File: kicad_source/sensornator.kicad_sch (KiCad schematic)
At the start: 23 parts, among them CN1 ARDUINO, CON1 Micro_SDCard, SW1 TAST_VER, SW2 TAST_VER, U5 ESP32_WROOM_32, U6 ATECC608A

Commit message: added qwiic connector
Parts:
- added CN2: SM04B-SRSS-TB, Connector_JST:JST_SH_SM04B-SRSS-TB_1x04-1MP_P1.00mm_Horizontal, symbol Connector_Generic:Conn_01x04
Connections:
- net +3V3: now also CN2.2 (Pin_2)
- net GND: now also CN2.1 (Pin_1)
- net I2C_SCL: now also CN2.4 (Pin_4)
- net I2C_SDA: now also CN2.3 (Pin_3)
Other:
- note added: "Copyright generationmake 2022 see full project documentation at https://github.com/generationmake/sensornator"
- note removed: "Copyright generationmake 2021 see full project documentation at https://github.com/generationmake/sensornator"
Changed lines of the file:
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@@
+    (stroke (width 0) (type default) (color 0 0 0 0))
+  )
+  (wire (pts (xy 73.66 41.91) (xy 97.79 41.91))
     (stroke (width 0) (type default) (color 0 0 0 0))
   )
@@
     (stroke (width 0) (type default) (color 0 0 0 0))
   )
+  (wire (pts (xy 92.71 39.37) (xy 92.71 34.29))
+    (stroke (width 0) (type default) (color 0 0 0 0))
+  )
   (wire (pts (xy 260.35 115.57) (xy 260.35 114.3))
     (stroke (width 0) (type default) (color 0 0 0 0))
@@
     (stroke (width 0) (type default) (color 0 0 0 0))
   )
+  (wire (pts (xy 97.79 39.37) (xy 92.71 39.37))
+    (stroke (width 0) (type default) (color 0 0 0 0))
+  )
   (wire (pts (xy 111.76 152.4) (xy 111.76 151.13))
     (stroke (width 0) (type default) (color 0 0 0 0))
@@
     (stroke (width 0) (type default) (color 0 0 0 0))
   )
+  (wire (pts (xy 97.79 36.83) (xy 95.25 36.83))
+    (stroke (width 0) (type default) (color 0 0 0 0))
+  )
   (wire (pts (xy 212.09 105.41) (xy 196.85 105.41))
     (stroke (width 0) (type default) (color 0 0 0 0))
@@
     (stroke (width 0) (type default) (color 0 0 0 0))
   )
+  (wire (pts (xy 73.66 44.45) (xy 97.79 44.45))
+    (stroke (width 0) (type default) (color 0 0 0 0))
+  )
   (wire (pts (xy 217.17 92.71) (xy 227.33 92.71))
     (stroke (width 0) (type default) (color 0 0 0 0))
@@
     (stroke (width 0) (type default) (color 0 0 0 0))
   )
+  (wire (pts (xy 95.25 36.83) (xy 95.25 46.99))
+    (stroke (width 0) (type default) (color 0 0 0 0))
+  )
   (wire (pts (xy 247.65 95.25) (xy 266.7 95.25))
     (stroke (width 0) (type default) (color 0 0 0 0))
@@
     (stroke (width 0) (type default) (color 0 0 0 0))
   )
-  (text "Copyright generationmake 2021\nsee full project documentation at https://github.com/generationmake/sensornator"
+  (text "Copyright generationmake 2022\nsee full project documentation at https://github.com/generationmake/sensornator"
     (at 12.7 16.51 0)
     (effects (font (size 1.1938 1.1938)) (justify left bottom))
@@
     (effects (font (size 1.524 1.524)) (justify left bottom))
   )
+  (label "I2C_SDA" (at 76.2 41.91 0)
+    (effects (font (size 1.524 1.524)) (justify left bottom))
+  )
   (label "EXT_RX" (at 250.19 85.09 0)
     (effects (font (size 1.524 1.524)) (justify left bottom))
@@
   )
   (label "ADC_1" (at 143.51 107.95 0)
+    (effects (font (size 1.524 1.524)) (justify left bottom))
+  )
+  (label "I2C_SCL" (at 76.2 44.45 0)
     (effects (font (size 1.524 1.524)) (justify left bottom))
   )
@@
     (pin "1")
   )
+  (symbol (lib_id "power:GND") (at 95.25 46.99 0) (unit 1)
+    (in_bom yes) (on_board yes)
+    (property "Reference" "#PWR012" (id 0) (at 95.25 53.34 0)
+      (effects (font (size 1.27 1.27)) hide)
+    )
+    (property "Value" "GND" (id 1) (at 95.25 50.8 0))
+    (property "Footprint" "" (id 2) (at 95.25 46.99 0))
+    (property "Datasheet" "" (id 3) (at 95.25 46.99 0))
+    (pin "1")
+  )
+  (symbol (lib_id "power:+3V3") (at 92.71 34.29 0) (unit 1)
+    (in_bom yes) (on_board yes)
+    (property "Reference" "#PWR011" (id 0) (at 92.71 38.1 0)
+      (effects (font (size 1.27 1.27)) hide)
+    )
+    (property "Value" "+3V3" (id 1) (at 93.091 31.0388 90)
+      (effects (font (size 1.27 1.27)) (justify left))
+    )
+    (property "Footprint" "" (id 2) (at 92.71 34.29 0))
+    (property "Datasheet" "" (id 3) (at 92.71 34.29 0))
+    (pin "1")
+  )
+  (symbol (lib_id "Connector_Generic:Conn_01x04") (at 102.87 39.37 0) (unit 1)
+    (in_bom yes) (on_board yes) (fields_autoplaced)
+    (property "Reference" "CN2" (id 0) (at 105.41 39.3699 0)
+      (effects (font (size 1.27 1.27)) (justify left))
+    )
+    (property "Value" "SM04B-SRSS-TB" (id 1) (at 105.41 41.9099 0)
+      (effects (font (size 1.27 1.27)) (justify left))
+    )
+    (property "Footprint" "Connector_JST:JST_SH_SM04B-SRSS-TB_1x04-1MP_P1.00mm_Horizontal" (id 2) (at 102.87 39.37 0)
+      (effects (font (size 1.27 1.27)) hide)
+    )
+    (property "Datasheet" "~" (id 3) (at 102.87 39.37 0)
+      (effects (font (size 1.27 1.27)) hide)
+    )
+    (pin "1")
+    (pin "2")
+    (pin "3")
+    (pin "4")
+  )
   (sheet (at 193.04 17.78) (size 21.59 15.24) (fields_autoplaced)
     (stroke (width 0) (type solid) (color 0 0 0 0))
@@
       (reference "#PWR010") (unit 1) (value "+3V3") (footprint "")
     )
+    (path "/723b0529-256e-4ea5-9e85-1d36b6678c46"
+      (reference "#PWR011") (unit 1) (value "+3V3") (footprint "")
+    )
+    (path "/1e42b0a4-ea04-4839-a101-ab6257e0d802"
+      (reference "#PWR012") (unit 1) (value "GND") (footprint "")
+    )
     (path "/00000000-0000-0000-0000-00005c166f4e"
       (reference "#PWR027") (unit 1) (value "GND") (footprint "")
@@
       (reference "CN1") (unit 1) (value "ARDUINO") (footprint "MODULE_compute:ARDUINO")
     )
+    (path "/f4d1e3aa-f75c-415b-af4a-76f49f7094e0"
+      (reference "CN2") (unit 1) (value "SM04B-SRSS-TB") (footprint "Connector_JST:JST_SH_SM04B-SRSS-TB_1x04-1MP_P1.00mm_Horizontal")
+    )
     (path "/00000000-0000-0000-0000-00005c166ac7"

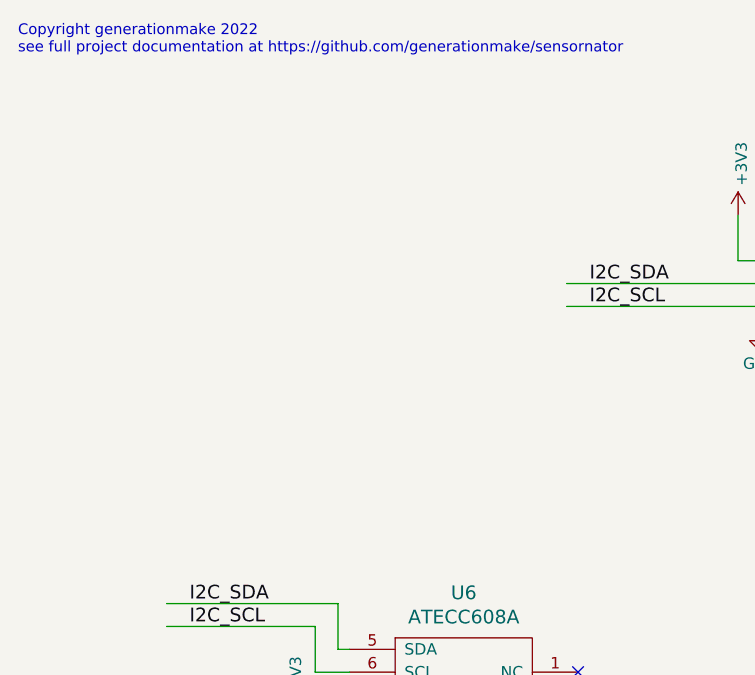
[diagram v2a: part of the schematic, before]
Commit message: added i2c eeprom
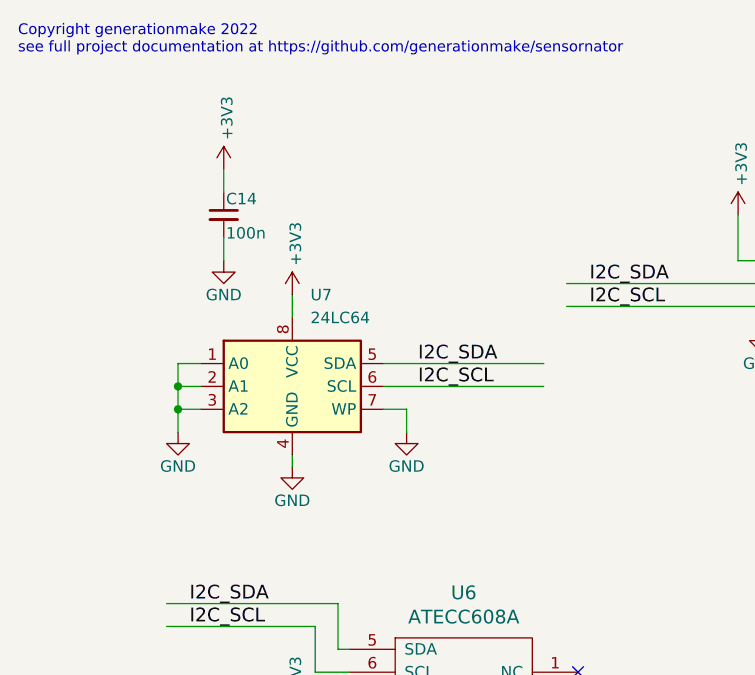
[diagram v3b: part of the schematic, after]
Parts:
- added C14: 100n, Capacitor_SMD:C_0603_1608Metric, symbol Device:C_Small
- added U7: 24LC64, Package_SO:SOIC-8_3.9x4.9mm_P1.27mm, symbol Memory_EEPROM:24LC64
- U6: footprint SOIC:SOIC-8_3.9x4.9mm_Pitch1.27mm -> Package_SO:SOIC-8_3.9x4.9mm_P1.27mm
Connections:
- net +3V3: now also C14.1, U7.8 (VCC)
- net GND: now also C14.2, U7.1 (A0), U7.2 (A1), U7.3 (A2), U7.4 (GND), U7.7 (WP)
- net I2C_SCL: now also U7.6 (SCL)
- net I2C_SDA: now also U7.5 (SDA)

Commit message: updated footprint libraries
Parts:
- C10, C11, C13, C8, C9: footprint capacitors:C_0603 -> Capacitor_SMD:C_0603_1608Metric
- D2: footprint LEDs:LED_0603 -> LED_SMD:LED_0603_1608Metric
- R11, R12, R13, R14, R15, R18, R19, R2, R20, R21, R8: footprint resistors:R_0603 -> Resistor_SMD:R_0603_1608Metric

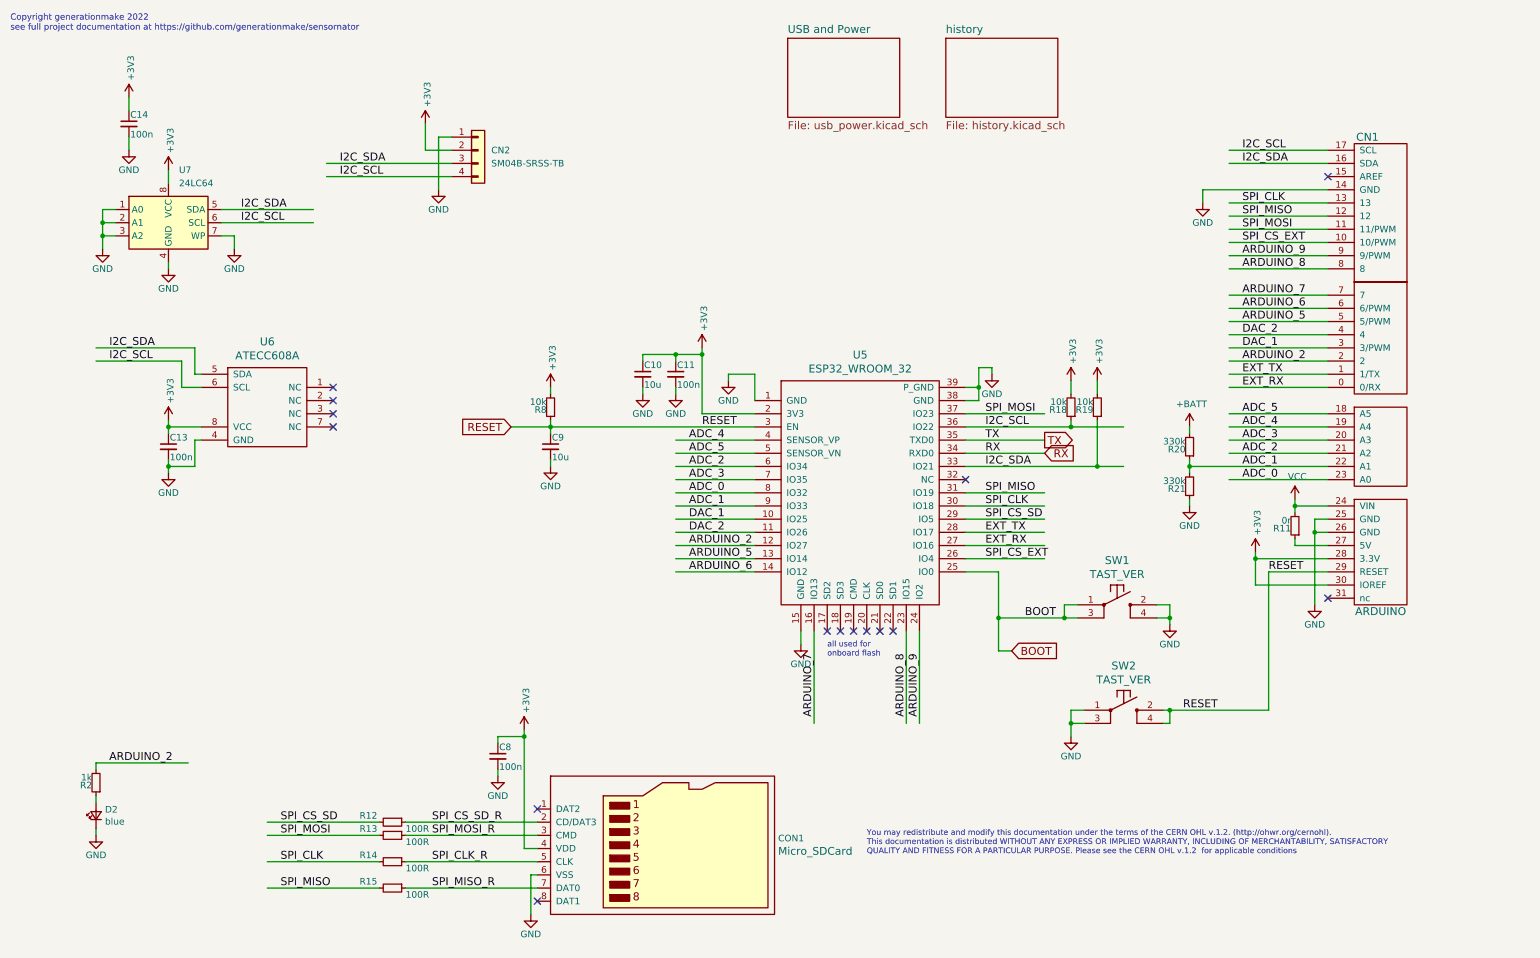
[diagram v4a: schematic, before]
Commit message: added CAN transceiver
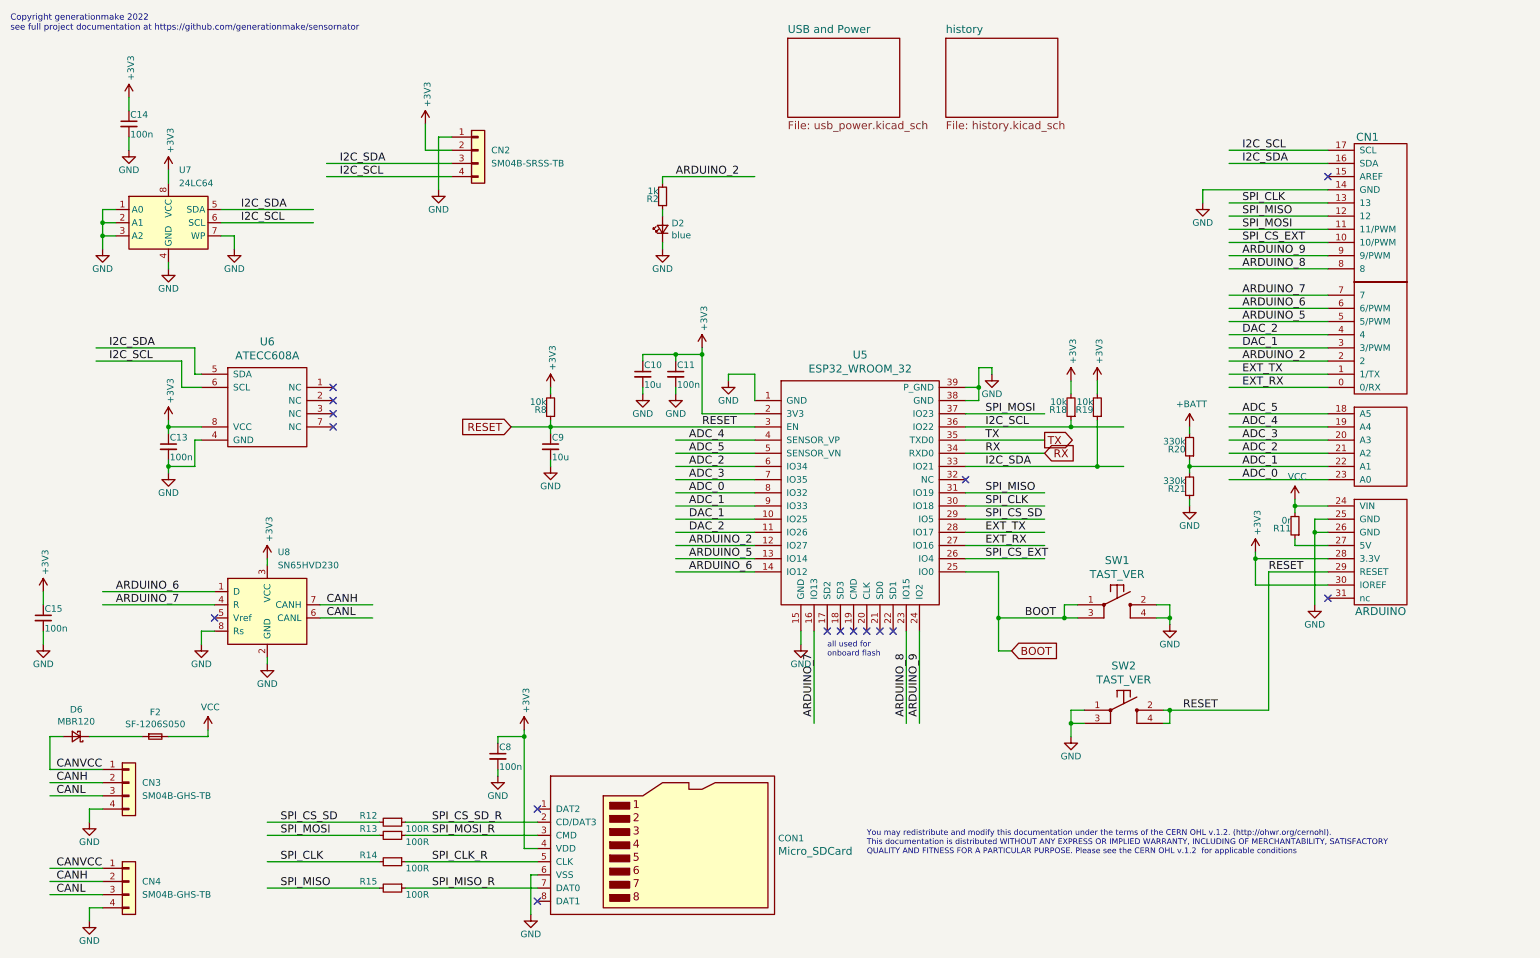
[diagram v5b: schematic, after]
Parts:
- added C15: 100n, Capacitor_SMD:C_0603_1608Metric, symbol Device:C_Small
- added CN3, CN4: SM04B-GHS-TB, Connector_JST:JST_GH_SM04B-GHS-TB_1x04-1MP_P1.25mm_Horizontal, symbol Connector_Generic:Conn_01x04
- added D6: MBR120, Diode_SMD:D_SOD-123, symbol Device:D_Schottky_Small
- added F2: SF-1206S050, Fuse:Fuse_1206_3216Metric, symbol Device:Fuse_Small
- added U8: SN65HVD230, Package_SO:SOIC-8_3.9x4.9mm_P1.27mm, symbol Interface_CAN_LIN:SN65HVD230
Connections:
- net +3V3: now also C15.1, U8.3 (VCC)
- net ARDUINO_6: now also U8.1 (D)
- net ARDUINO_7: now also U8.4 (R)
- net GND: now also C15.2, CN3.4 (Pin_4), CN4.4 (Pin_4), U8.2 (GND), U8.8 (Rs)
- net VCC: now also F2.2
- new net: D6.1 (K), F2.1
- new net CANH: CN3.2 (Pin_2), CN4.2 (Pin_2), U8.7 (CANH)
- new net CANL: CN3.3 (Pin_3), CN4.3 (Pin_3), U8.6 (CANL)
- new net CANVCC: CN3.1 (Pin_1), CN4.1 (Pin_1), D6.2 (A)
- no-connect marks 15 -> 16
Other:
- moved on the sheet: D2, R2

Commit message: added mounting pins on connectors, added labels
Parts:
- removed CN2: SM04B-SRSS-TB, Connector_JST:JST_SH_SM04B-SRSS-TB_1x04-1MP_P1.00mm_Horizontal, symbol Connector_Generic:Conn_01x04
- removed CN3, CN4: SM04B-GHS-TB, Connector_JST:JST_GH_SM04B-GHS-TB_1x04-1MP_P1.25mm_Horizontal, symbol Connector_Generic:Conn_01x04
- added CN2: SM04B-SRSS-TB, Connector_JST:JST_SH_SM04B-SRSS-TB_1x04-1MP_P1.00mm_Horizontal, symbol Connector_Generic_MountingPin:Conn_01x04_MountingPin
- added CN3, CN4: SM04B-GHS-TB, Connector_JST:JST_GH_SM04B-GHS-TB_1x04-1MP_P1.25mm_Horizontal, symbol Connector_Generic_MountingPin:Conn_01x04_MountingPin
- added L1, L2: Label, generationmake:generationmake_logo, symbol generationmake:Label
- added L3: Label, Symbol:OSHW-Symbol_8.9x8mm_SilkScreen, symbol generationmake:Label
- added L4: Label, generationmake:opencyphal_small, symbol generationmake:Label
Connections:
- net +3V3: now also CN2.2 (Pin_2)
- net CANH: now also CN3.2 (Pin_2), CN4.2 (Pin_2)
- net CANL: now also CN3.3 (Pin_3), CN4.3 (Pin_3)
- net CANVCC: now also CN3.1 (Pin_1), CN4.1 (Pin_1)
- net GND: now also CN2.1 (Pin_1), CN3.4 (Pin_4), CN4.4 (Pin_4)
- net I2C_SCL: now also CN2.4 (Pin_4)
- net I2C_SDA: now also CN2.3 (Pin_3)
- new net MP: CN3.MP (MountPin), CN4.MP (MountPin)
- new net MP_2: CN2.MP (MountPin)
